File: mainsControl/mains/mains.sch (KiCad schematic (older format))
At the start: 10 parts

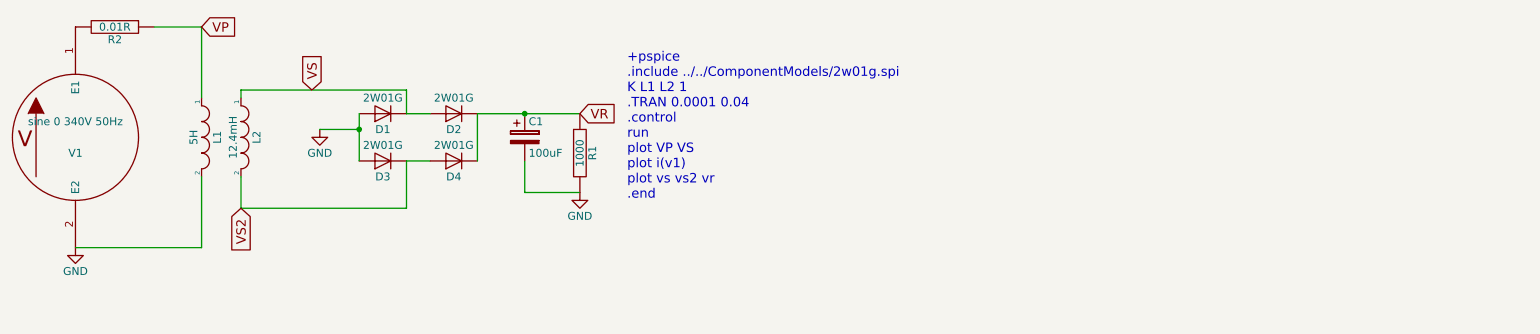
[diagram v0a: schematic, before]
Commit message: mains circuit working
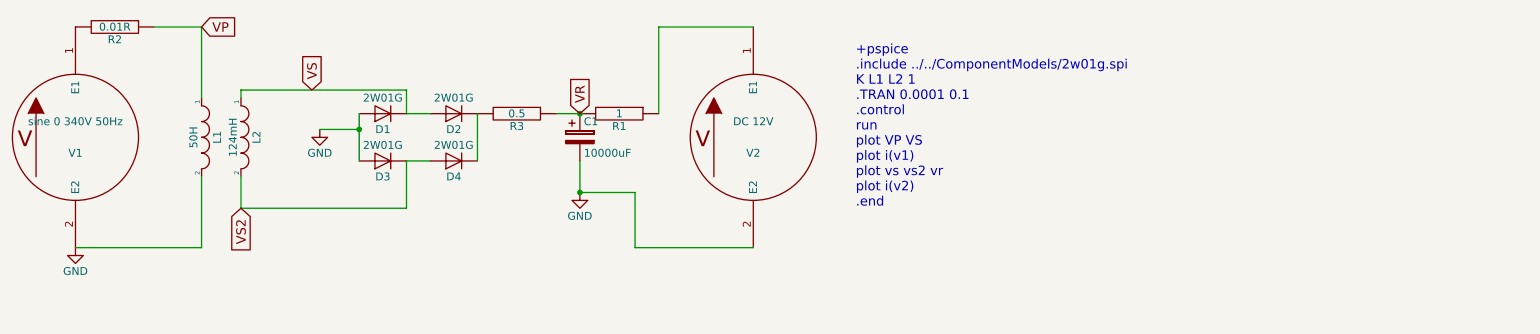
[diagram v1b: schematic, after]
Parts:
- added R3: 0.5, symbol R
- added V2: DC 12V, symbol VSOURCE
- C1: value 100uF -> 10000uF
- L1: value 5H -> 50H
- L2: value 12.4mH -> 124mH
- R1: value 1000 -> 1
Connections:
- net GND: now also V2.2 (E2); no longer R1.2
- net VR: now also R1.2, R3.1; no longer D2.1 (K), D4.1 (K), R1.1
- new net: R1.1, V2.1 (E1)
- new net: D2.1 (K), D4.1 (K), R3.2
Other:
- note added: "+pspice\n.include ../../ComponentModels/2w01g.spi\nK L1 L2 1\n.TRAN 0.0001 0.1\n.control\nrun\nplot VP VS\nplot i(v1)\nplot vs vs2 vr\nplot i(v2)\n.end"
- note removed: "+pspice\n.include ../../ComponentModels/2w01g.spi\nK L1 L2 1\n.TRAN 0.0001 0.04\n.control\nrun\nplot VP VS\nplot i(v1)\nplot vs vs2 vr\n.end"
- moved on the sheet: C1, R1
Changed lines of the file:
@@
 	1    0    0    -1
 $EndComp
-Text Notes 4400 1850 0    60   ~ 0
-+pspice\n.include ../../ComponentModels/2w01g.spi\nK L1 L2 1\n.TRAN 0.0001 0.04\n.control\nrun\nplot VP VS\nplot i(v1)\nplot vs vs2 vr\n.end
+Text Notes 5850 1900 0    60   ~ 0
++pspice\n.include ../../ComponentModels/2w01g.spi\nK L1 L2 1\n.TRAN 0.0001 0.1\n.control\nrun\nplot VP VS\nplot i(v1)\nplot vs vs2 vr\nplot i(v2)\n.end
 $Comp
 L INDUCTOR L1
@@
 P 1700 1450
 F 0 "L1" H 1700 1550 50  0000 C CNN
-F 1 "5H" H 1700 1400 50  0000 C CNN
+F 1 "50H" H 1700 1400 50  0000 C CNN
 F 2 "" H 1700 1450 50  0001 C CNN
 F 3 "" H 1700 1450 50  0001 C CNN
@@
 P 1950 1450
 F 0 "L2" H 1950 1550 50  0000 C CNN
-F 1 "12.4mH " H 1950 1400 50  0000 C CNN
+F 1 "124mH " H 1950 1400 50  0000 C CNN
 F 2 "" H 1950 1450 50  0001 C CNN
 F 3 "" H 1950 1450 50  0001 C CNN
@@
 L R R1
 U 1 1 5AFC6729
-P 4100 1550
-F 0 "R1" V 4180 1550 50  0000 C CNN
-F 1 "1000" V 4100 1550 50  0000 C CNN
-F 2 "" H 4100 1550 50  0001 C CNN
-F 3 "" H 4100 1550 50  0001 C CNN
-	1    4100 1550
-	1    0    0    -1
+P 4350 1300
+F 0 "R1" V 4430 1300 50  0000 C CNN
+F 1 "1" V 4350 1300 50  0000 C CNN
+F 2 "" H 4350 1300 50  0001 C CNN
+F 3 "" H 4350 1300 50  0001 C CNN
+	1    4350 1300
+	0    1    1    0
 $EndComp
 Text GLabel 2400 1150 1    60   Input ~ 0
@@
 	3000 1150 3000 1300
 Wire Wire Line
-	4100 1300 3450 1300
+	3950 1300 4100 1300
 Wire Wire Line
 	3450 1300 3450 1600
@@
 Wire Wire Line
 	1950 1200 1950 1150
-Text GLabel 4100 1300 2    60   Input ~ 0
+Text GLabel 4100 1300 1    60   Input ~ 0
 VR
 Text GLabel 1950 1900 3    60   Input ~ 0
@@
 L CP C1
 U 1 1 5B025FCF
-P 3750 1450
-F 0 "C1" H 3775 1550 50  0000 L CNN
-F 1 "100uF" H 3775 1350 50  0000 L CNN
-F 2 "" H 3788 1300 50  0001 C CNN
-F 3 "" H 3750 1450 50  0001 C CNN
-	1    3750 1450
+P 4100 1450
+F 0 "C1" H 4125 1550 50  0000 L CNN
+F 1 "10000uF" H 4125 1350 50  0000 L CNN
+F 2 "" H 4138 1300 50  0001 C CNN
+F 3 "" H 4100 1450 50  0001 C CNN
+	1    4100 1450
 	1    0    0    -1
 $EndComp
 Wire Wire Line
-	3750 1600 3750 1800
+	4100 1600 4100 1800
 Wire Wire Line
-	3750 1800 4100 1800
-Connection ~ 3750 1300
+	4100 1800 4450 1800
+Connection ~ 4100 1300
 $Comp
-L GND #PWR02
+L GND #PWR03
 U 1 1 5AFC694D
 P 900 2150
-F 0 "#PWR02" H 900 1900 50  0001 C CNN
+F 0 "#PWR03" H 900 1900 50  0001 C CNN
 F 1 "GND" H 900 2000 50  0000 C CNN
 F 2 "" H 900 2150 50  0001 C CNN
@@
 	1    0    0    -1
 $EndComp
+$Comp
+L VSOURCE V2
+U 1 1 5B02AC3F
+P 5200 1450
+F 0 "V2" H 5200 1350 50  0000 C CNN
+F 1 "DC 12V " H 5200 1550 50  0000 C CNN
+F 2 "" H 5200 1450 50  0001 C CNN
+F 3 "" H 5200 1450 50  0001 C CNN
+	1    5200 1450
+	1    0    0    -1
+$EndComp
+Wire Wire Line
+	5200 2150 4450 2150
+Wire Wire Line
+	4450 2150 4450 1800
+Connection ~ 4100 1800
+Wire Wire Line
+	5200 750  4600 750
+Wire Wire Line
+	4600 750  4600 1300
+$Comp
+L R R3
+U 1 1 5B02AE67
+P 3700 1300
+F 0 "R3" V 3780 1300 50  0000 C CNN
+F 1 "0.5" V 3700 1300 50  0000 C CNN
+F 2 "" H 3700 1300 50  0001 C CNN
+F 3 "" H 3700 1300 50  0001 C CNN
+	1    3700 1300
+	0    1    1    0
+$EndComp
 $EndSCHEMATC

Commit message: added bridge rectifier GBJ1506
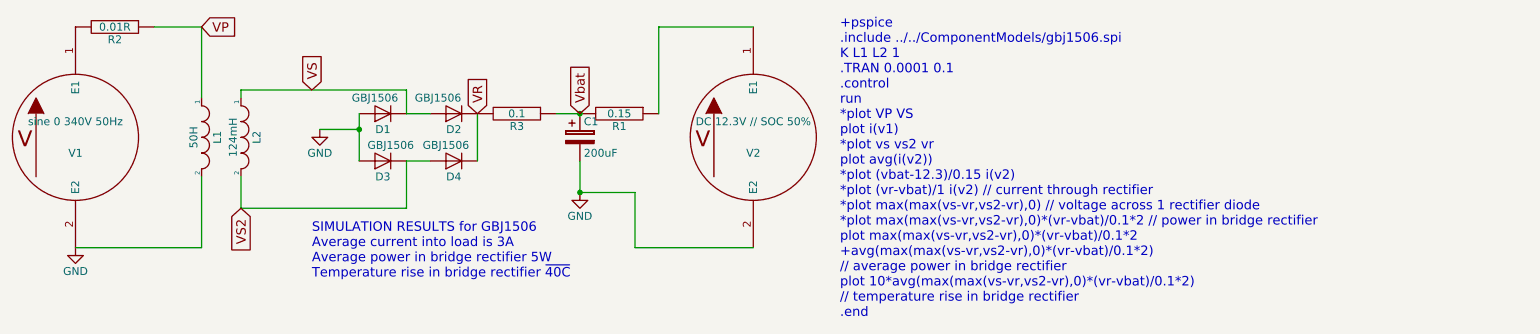
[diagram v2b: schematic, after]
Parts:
- C1: value 10000uF -> 200uF
- D1, D2, D3, D4: value 2W01G -> GBJ1506
- R1: value 1 -> 0.15
- R3: value 0.5 -> 0.1
- V2: value DC 12V -> DC 12.3V // SOC 50%
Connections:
- net VR: now also D2.1 (K), D4.1 (K), R3.2; no longer C1.1, R1.2, R3.1
- new net Vbat: C1.1, R1.2, R3.1
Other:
- note added: "+pspice\n.include ../../ComponentModels/gbj1506.spi\nK L1 L2 1\n.TRAN 0.0001 0.1 \n.control\nrun\n*plot VP VS\nplot i(v1)\n*plot vs vs2 vr\nplot avg(i(v2))\n*plot (vbat-12.3)/0.15 i(v2)\n*plot (vr-vbat)/1 i(v2) // current through rectifier\n*plot max(max(vs-vr,vs2-vr),0) // voltage across 1 rectifier diode\n*plot max(max(vs-vr,vs2-vr),0)*(vr-vbat)/0.1*2 // power in bridge rectifier\nplot max(max(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"
- note added: "SIMULATION RESULTS for GBJ1506\nAverage current into load is 3A\nAverage power in bridge rectifier 5W\nTemperature rise in bridge rectifier ~40C"
- note removed: "+pspice\n.include ../../ComponentModels/2w01g.spi\nK L1 L2 1\n.TRAN 0.0001 0.1\n.control\nrun\nplot VP VS\nplot i(v1)\nplot vs vs2 vr\nplot i(v2)\n.end"
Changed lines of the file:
@@
 	1    0    0    -1
 $EndComp
-Text Notes 5850 1900 0    60   ~ 0
-+pspice\n.include ../../ComponentModels/2w01g.spi\nK L1 L2 1\n.TRAN 0.0001 0.1\n.control\nrun\nplot VP VS\nplot i(v1)\nplot vs vs2 vr\nplot i(v2)\n.end
+Text Notes 5750 2600 0    60   ~ 0
++pspice\n.include ../../ComponentModels/gbj1506.spi\nK L1 L2 1\n.TRAN 0.0001 0.1 \n.control\nrun\n*plot VP VS\nplot i(v1)\n*plot vs vs2 vr\nplot avg(i(v2))\n*plot (vbat-12.3)/0.15 i(v2)\n*plot (vr-vbat)/1 i(v2) // current through rectifier\n*plot max(max(vs-vr,vs2-vr),0) // voltage across 1 rectifier diode\n*plot max(max(vs-vr,vs2-vr),0)*(vr-vbat)/0.1*2 // power in bridge rectifier\nplot max(max(vs-vr,vs2-vr),0)*(vr-vbat)/0.1*2 \n+avg(max(max(vs-vr,vs2-vr),0)*(vr-vbat)/0.1*2) \n// average power in bridge rectifier\nplot 10*avg(max(max(vs-vr,vs2-vr),0)*(vr-vbat)/0.1*2) \n// temperature rise in bridge rectifier\n.end
 $Comp
 L INDUCTOR L1
@@
 P 4350 1300
 F 0 "R1" V 4430 1300 50  0000 C CNN
-F 1 "1" V 4350 1300 50  0000 C CNN
+F 1 "0.15" V 4350 1300 50  0000 C CNN
 F 2 "" H 4350 1300 50  0001 C CNN
 F 3 "" H 4350 1300 50  0001 C CNN
@@
 P 2850 1300
 F 0 "D1" H 2850 1400 50  0000 C CNN
-F 1 "2W01G" H 2850 1200 50  0000 C CNN
+F 1 "GBJ1506" H 2900 1200 50  0000 C CNN
 F 2 "" H 2850 1300 50  0001 C CNN
 F 3 "" H 2850 1300 50  0001 C CNN
@@
 P 2850 1600
 F 0 "D3" H 2850 1700 50  0000 C CNN
-F 1 "2W01G" H 2850 1500 50  0000 C CNN
+F 1 "GBJ1506" H 2800 1500 50  0000 C CNN
 F 2 "" H 2850 1600 50  0001 C CNN
 F 3 "" H 2850 1600 50  0001 C CNN
@@
 P 3300 1300
 F 0 "D2" H 3300 1400 50  0000 C CNN
-F 1 "2W01G" H 3300 1200 50  0000 C CNN
+F 1 "GBJ1506" H 3400 1200 50  0000 C CNN
 F 2 "" H 3300 1300 50  0001 C CNN
 F 3 "" H 3300 1300 50  0001 C CNN
@@
 P 3300 1600
 F 0 "D4" H 3300 1700 50  0000 C CNN
-F 1 "2W01G" H 3300 1500 50  0000 C CNN
+F 1 "GBJ1506" H 3350 1500 50  0000 C CNN
 F 2 "" H 3300 1600 50  0001 C CNN
 F 3 "" H 3300 1600 50  0001 C CNN
@@
 	1950 1200 1950 1150
 Text GLabel 4100 1300 1    60   Input ~ 0
-VR
+Vbat
 Text GLabel 1950 1900 3    60   Input ~ 0
 VS2
@@
 P 4100 1450
 F 0 "C1" H 4125 1550 50  0000 L CNN
-F 1 "10000uF" H 4125 1350 50  0000 L CNN
+F 1 "200uF" H 4125 1350 50  0000 L CNN
 F 2 "" H 4138 1300 50  0001 C CNN
 F 3 "" H 4100 1450 50  0001 C CNN
@@
 P 5200 1450
 F 0 "V2" H 5200 1350 50  0000 C CNN
-F 1 "DC 12V " H 5200 1550 50  0000 C CNN
+F 1 "DC 12.3V // SOC 50%" H 5200 1550 50  0000 C CNN
 F 2 "" H 5200 1450 50  0001 C CNN
 F 3 "" H 5200 1450 50  0001 C CNN
@@
 P 3700 1300
 F 0 "R3" V 3780 1300 50  0000 C CNN
-F 1 "0.5" V 3700 1300 50  0000 C CNN
+F 1 "0.1" V 3700 1300 50  0000 C CNN
 F 2 "" H 3700 1300 50  0001 C CNN
 F 3 "" H 3700 1300 50  0001 C CNN
@@
 	0    1    1    0
 $EndComp
+Text GLabel 3450 1300 1    60   Input ~ 0
+VR
+Text Notes 2400 2350 0    60   ~ 0
+SIMULATION RESULTS for GBJ1506\nAverage current into load is 3A\nAverage power in bridge rectifier 5W\nTemperature rise in bridge rectifier ~40C
 $EndSCHEMATC
